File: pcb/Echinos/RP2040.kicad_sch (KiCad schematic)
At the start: 19 parts, among them U2 RP2040, X1 ASE-12MHz

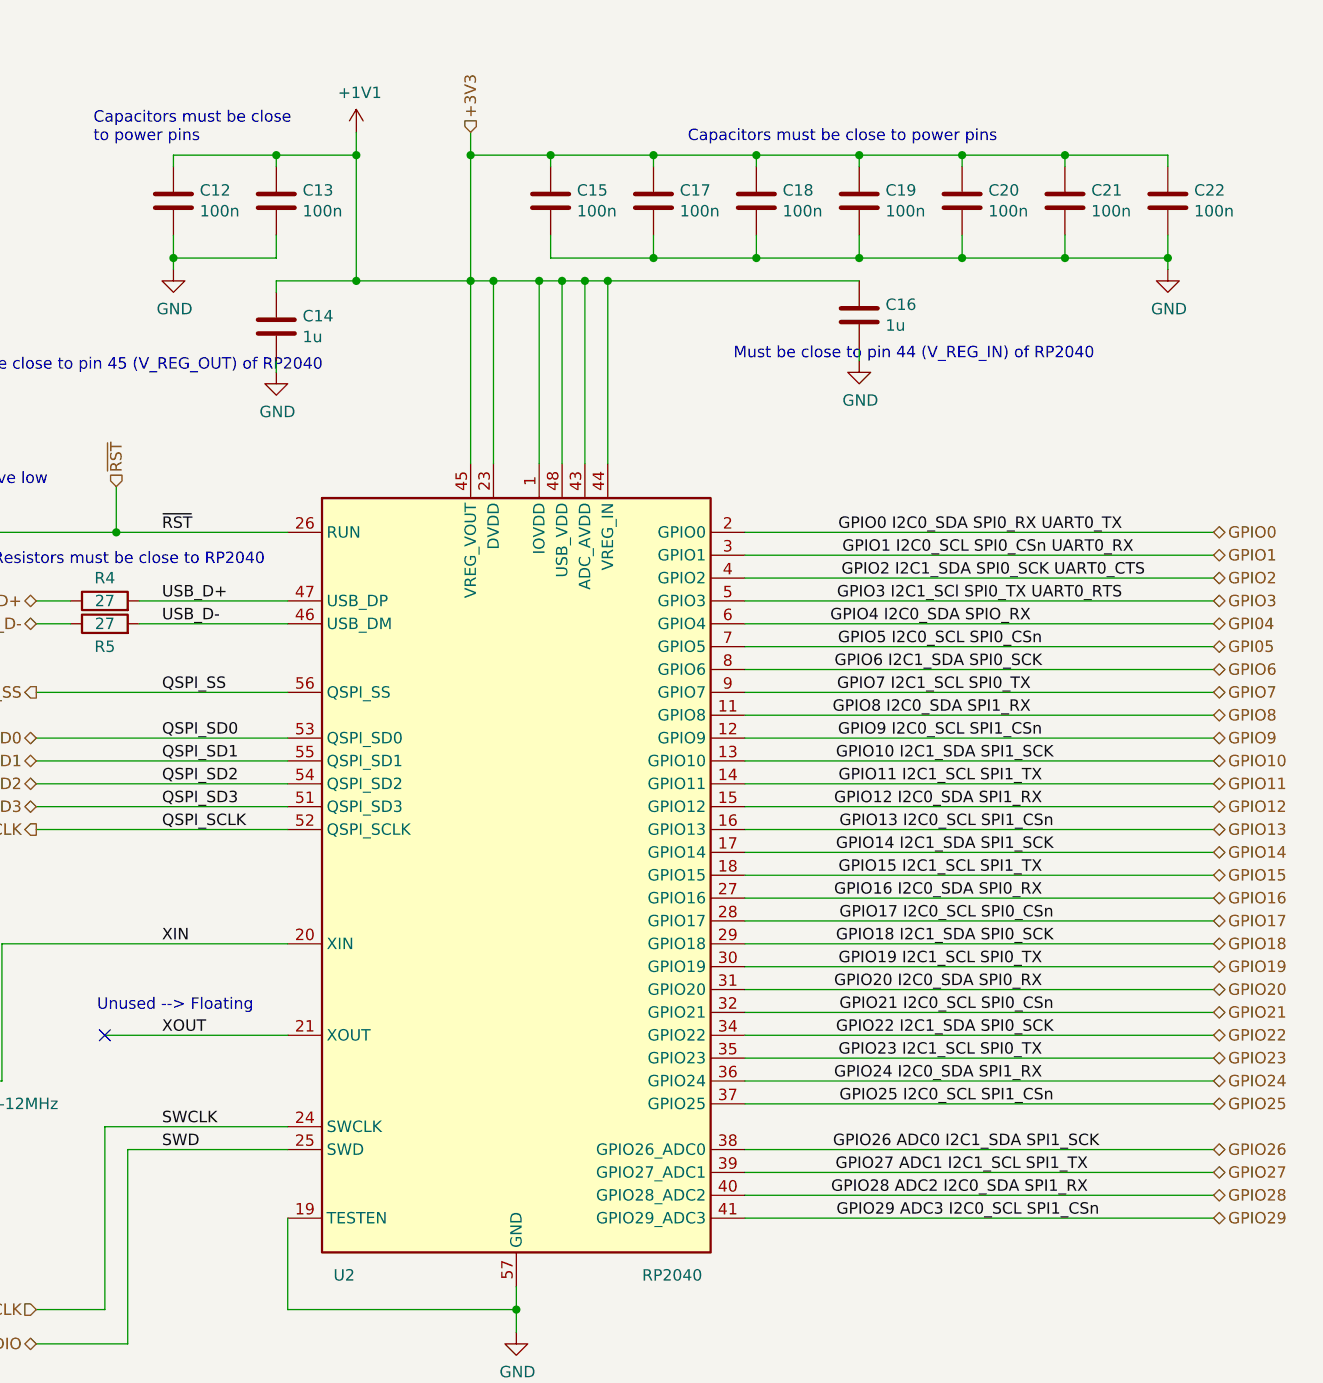
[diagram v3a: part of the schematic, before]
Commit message: ✨ 🐛 ✅ [PCB] - Pass ERC test (exception to unconnected GPIO pins). Fix power symbol assignation to please Kicad. Fix duplicated line name (encoder / joystick) to please Kicad. Add trackball sensor connection documentation. Assign newly created footprints (encoder, joystick, switch).
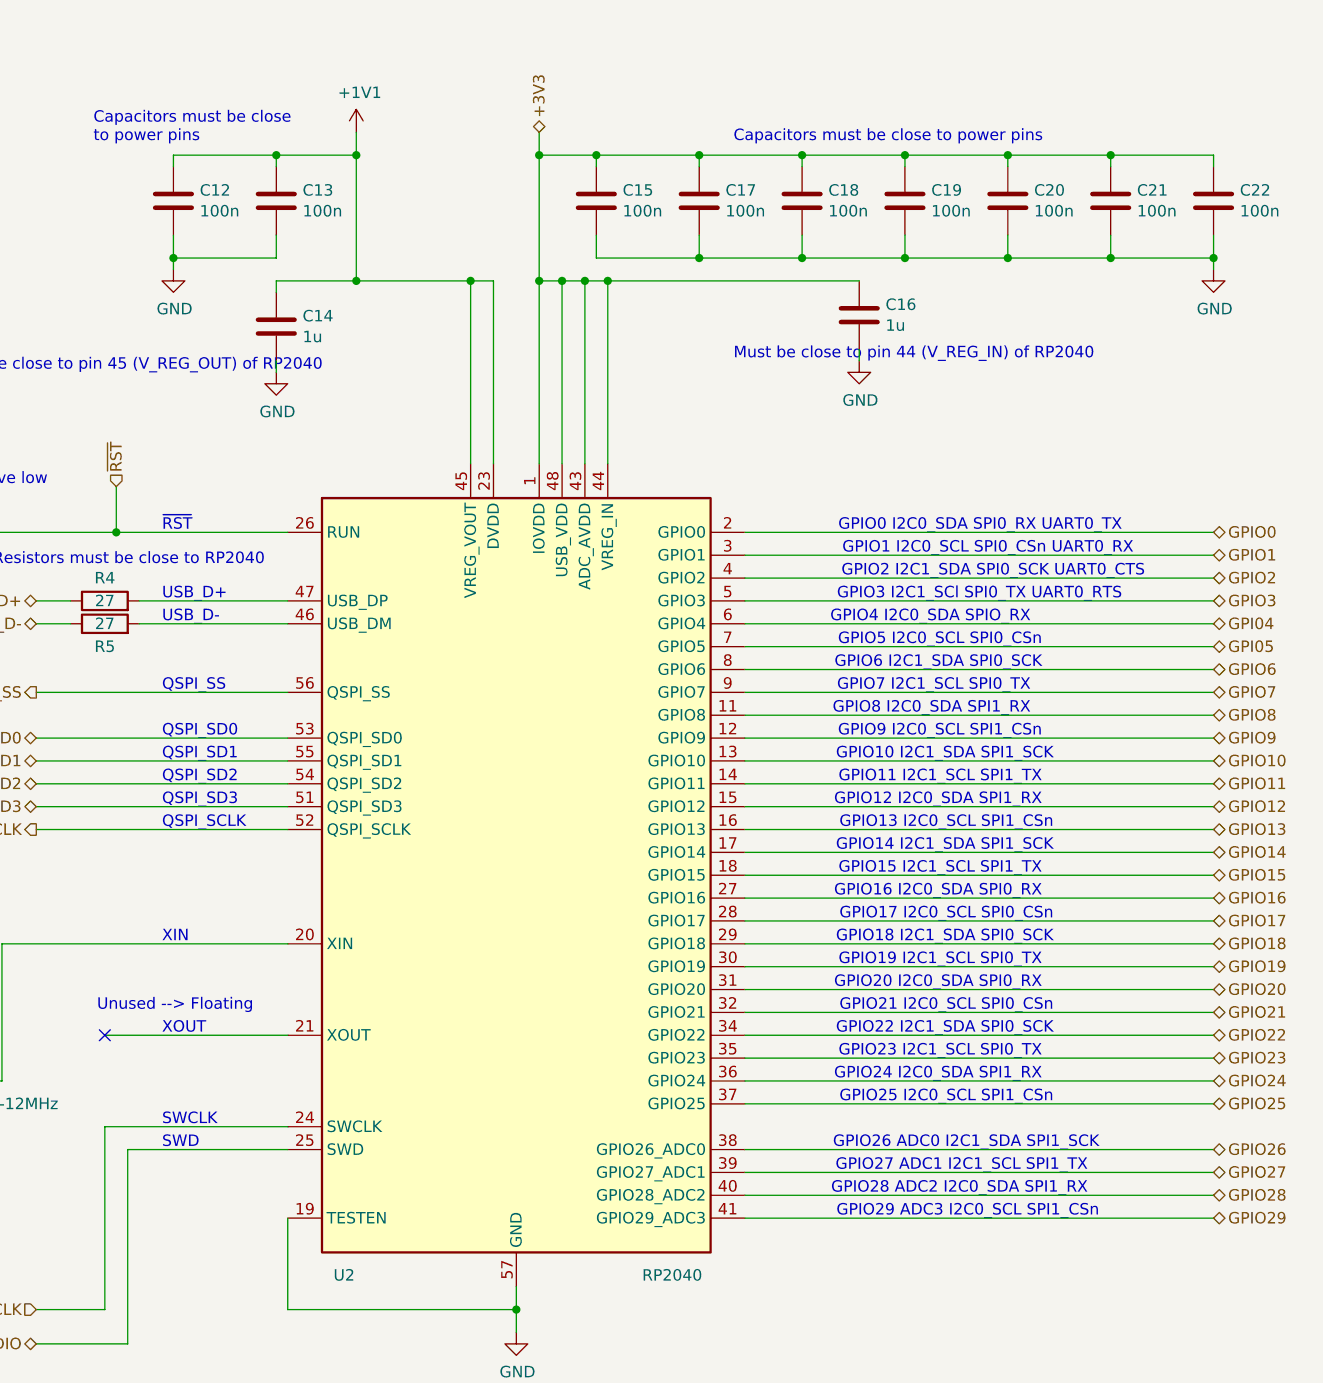
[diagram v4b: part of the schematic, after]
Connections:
- net +1V1: no longer C14.1, C15.1, C16.1, C17.1, C18.1, C19.1, C20.1, C21.1, C22.1, R4.2, R7.1, U2.1 (IOVDD), U2.10 (IOVDD), U2.22 (IOVDD), U2.33 (IOVDD), U2.42 (IOVDD), U2.43 (ADC_AVDD), U2.44 (VREG_IN), U2.48 (USB_VDD), U2.49 (IOVDD), X1.4 (Vdd)
- net USB_D+: no longer R4.2, U2.47 (USB_DP)
- net USB_D-: no longer R5.2, U2.46 (USB_DM)
- net XIN: no longer names the net of U2.20 (XIN), X1.3 (OUT)
- net XOUT: no longer names the net of U2.21 (XOUT)
- new net: R5.2, U2.46 (USB_DM)
- new net: R4.2, U2.47 (USB_DP)
- new net +3V3: C14.1, C15.1, C16.1, C17.1, C18.1, C19.1, C20.1, C21.1, C22.1, R4.2, R7.1, U2.1 (IOVDD), U2.10 (IOVDD), U2.22 (IOVDD), U2.33 (IOVDD), U2.42 (IOVDD), U2.43 (ADC_AVDD), U2.44 (VREG_IN), U2.48 (USB_VDD), U2.49 (IOVDD), X1.4 (Vdd)
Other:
- note added: "GPIO0 I2C0_SDA SPI0_RX UART0_TX"
- note added: "GPIO1 I2C0_SCL SPI0_CSn UART0_RX"
- note added: "GPIO10 I2C1_SDA SPI1_SCK"
- note added: "GPIO11 I2C1_SCL SPI1_TX"
- note added: "GPIO12 I2C0_SDA SPI1_RX"
- note added: "GPIO13 I2C0_SCL SPI1_CSn"
- note added: "GPIO14 I2C1_SDA SPI1_SCK"
- note added: "GPIO15 I2C1_SCL SPI1_TX"
- note added: "GPIO16 I2C0_SDA SPI0_RX"
- note added: "GPIO17 I2C0_SCL SPI0_CSn"
- note added: "GPIO18 I2C1_SDA SPI0_SCK"
- note added: "GPIO19 I2C1_SCL SPI0_TX"
- note added: "GPIO2 I2C1_SDA SPI0_SCK UART0_CTS"
- note added: "GPIO20 I2C0_SDA SPI0_RX"
- note added: "GPIO21 I2C0_SCL SPI0_CSn"
- note added: "GPIO22 I2C1_SDA SPI0_SCK"
- note added: "GPIO23 I2C1_SCL SPI0_TX"
- note added: "GPIO24 I2C0_SDA SPI1_RX"
- note added: "GPIO25 I2C0_SCL SPI1_CSn"
- note added: "GPIO26 ADC0 I2C1_SDA SPI1_SCK"
- note added: "GPIO27 ADC1 I2C1_SCL SPI1_TX"
- note added: "GPIO28 ADC2 I2C0_SDA SPI1_RX"
- note added: "GPIO29 ADC3 I2C0_SCL SPI1_CSn"
- note added: "GPIO3 I2C1_SCl SPI0_TX UART0_RTS"
- note added: "GPIO4 I2C0_SDA SPIO_RX"
- note added: "GPIO5 I2C0_SCL SPI0_CSn"
- note added: "GPIO6 I2C1_SDA SPI0_SCK"
- note added: "GPIO7 I2C1_SCL SPI0_TX"
- note added: "GPIO8 I2C0_SDA SPI1_RX"
- note added: "GPIO9 I2C0_SCL SPI1_CSn"
- note added: "QSPI_SCLK"
- note added: "QSPI_SD0"
- note added: "QSPI_SD1"
- note added: "QSPI_SD2"
- note added: "QSPI_SD3"
- note added: "QSPI_SS"
- note added: "SWCLK"
- note added: "SWD"
- note added: "USB_D+"
- note added: "USB_D-"
- note added: "XIN"
- note added: "XOUT"
- note added: "~{RST}"
- moved on the sheet: C15, C17, C18, C19, C20, C21, C22

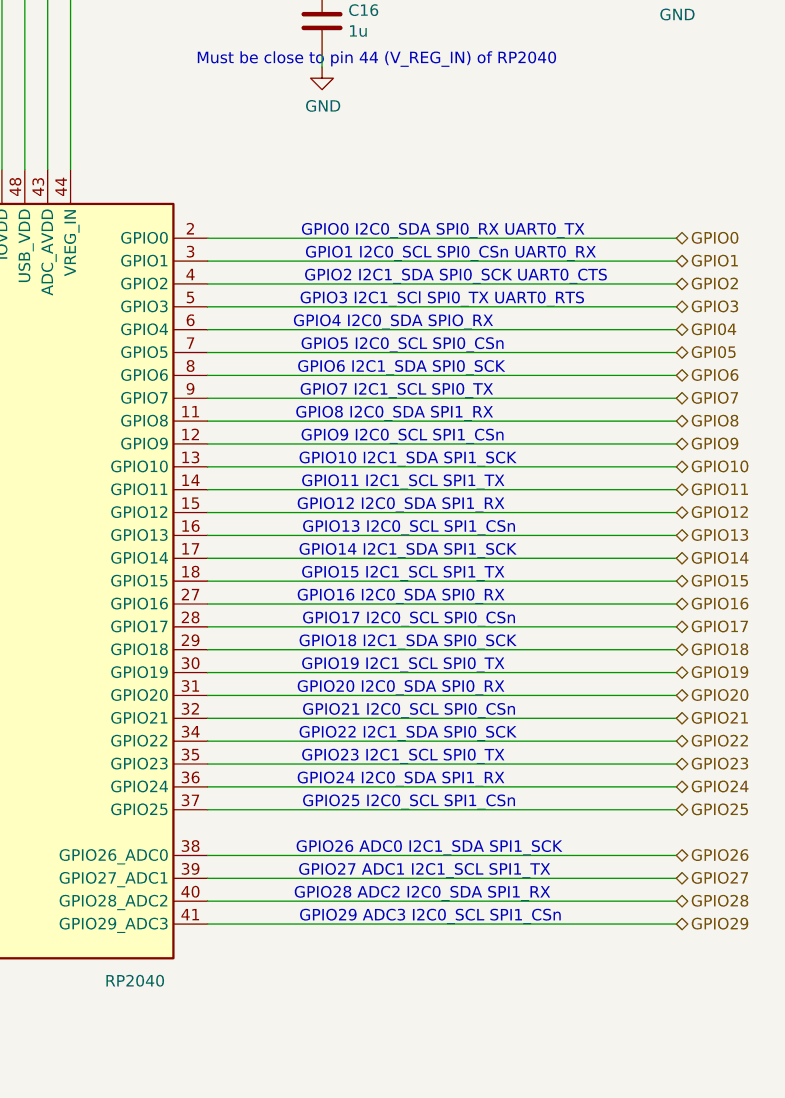
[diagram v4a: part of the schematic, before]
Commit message: ✨ [PCB] - Complete schema and PCB for left halve. All connections are made. Optional encoder on the top outer key Optional joystick on either outer thumb or above middle thumb. Optional power LED (jumpers) SATA to connect both sides VIK compatible (except for 5.0V track) with enough space on the inner side to clip a VIK module Remaining MCU pins exposed with a 2.54mm spaced header All VIK modules are not yet placed / routed.
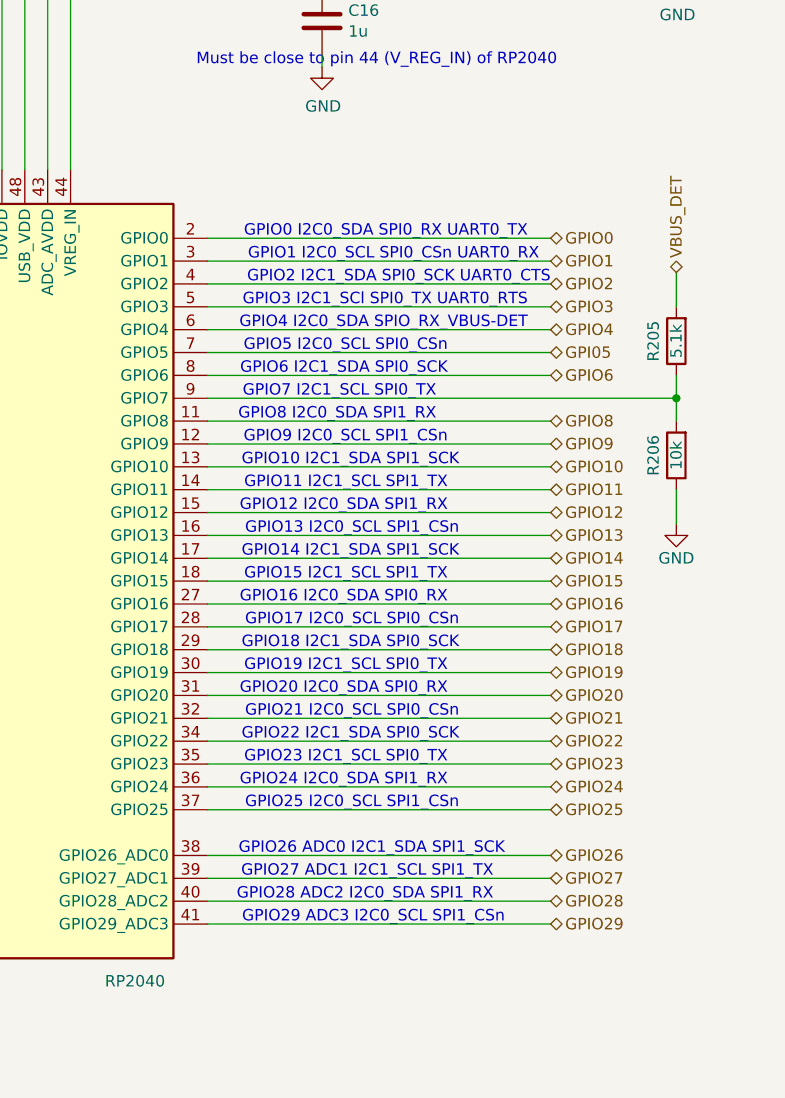
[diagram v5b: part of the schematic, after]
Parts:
- added R205: 5.1k, Resistor_SMD:R_0402_1005Metric_Pad0.72x0.64mm_HandSolder, symbol Device:R
- added R206: 10k, Resistor_SMD:R_0402_1005Metric_Pad0.72x0.64mm_HandSolder, symbol Device:R
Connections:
- net GND: now also R206.1
- net GPI04 renamed GPIO4
- net GPIO7: no longer names the net of U2.9 (GPIO7)
- net GPIO7: now also R205.1, R206.2
- new net VBUS_DET: R205.2
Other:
- note added: "GPIO4 I2C0_SDA SPIO_RX_VBUS-DET"
- note removed: "GPIO4 I2C0_SDA SPIO_RX"

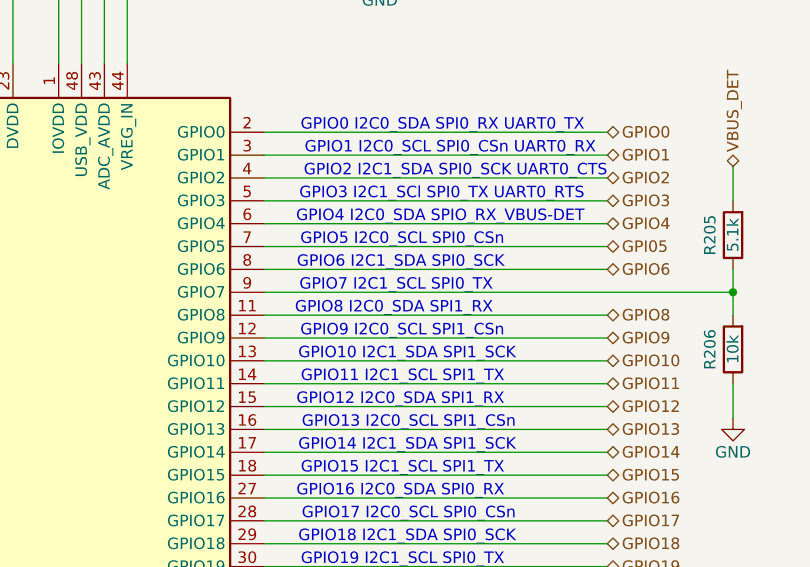
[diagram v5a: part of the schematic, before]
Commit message: ✨ [PCB] - Make some place to add a FPC connector providing a way to expand the matrix / number of keys or add a joystick and I2C pull-up resistors. Improve routing in order to minimize the number of vias.
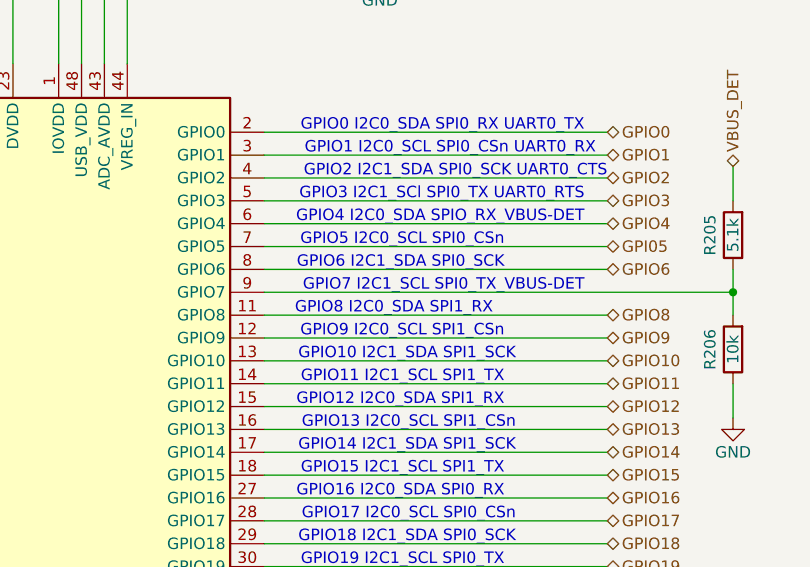
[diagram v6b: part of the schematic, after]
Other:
- note added: "GPIO7 I2C1_SCL SPI0_TX_VBUS-DET"
- note removed: "GPIO7 I2C1_SCL SPI0_TX"
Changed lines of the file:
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@@
     (effects (font (size 1.27 1.27)) (justify right bottom))
   )
-  (text "GPIO7 I2C1_SCL SPI0_TX" (at 247.65 87.63 0)
+  (text "GPIO7 I2C1_SCL SPI0_TX_VBUS-DET" (at 257.81 87.63 0)
     (effects (font (size 1.27 1.27)) (justify right bottom))
   )
